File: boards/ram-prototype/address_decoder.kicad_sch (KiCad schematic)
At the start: 33 parts, among them U1 74LVC1G04, U10 74LVC1G11, U11 74LVC1G11, U2 74LVC1G04, U3 74LVC1G04, U4 74LVC1G11, U5 74LVC1G11, U6 74LVC1G11, U7 74LVC1G11, U8 74LVC1G11, U9 74LVC1G11

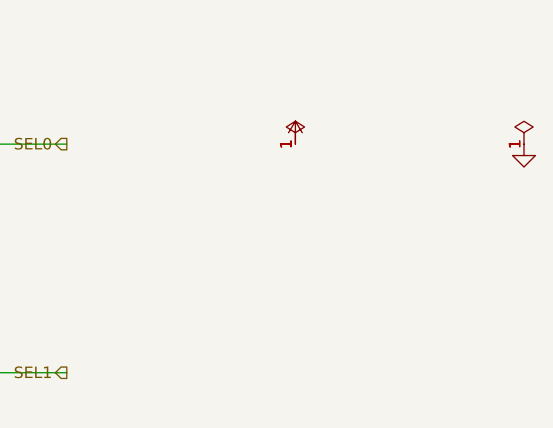
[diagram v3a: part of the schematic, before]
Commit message: More reasonable top level designrout
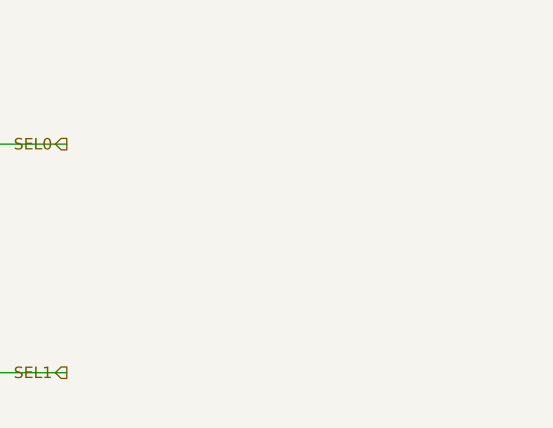
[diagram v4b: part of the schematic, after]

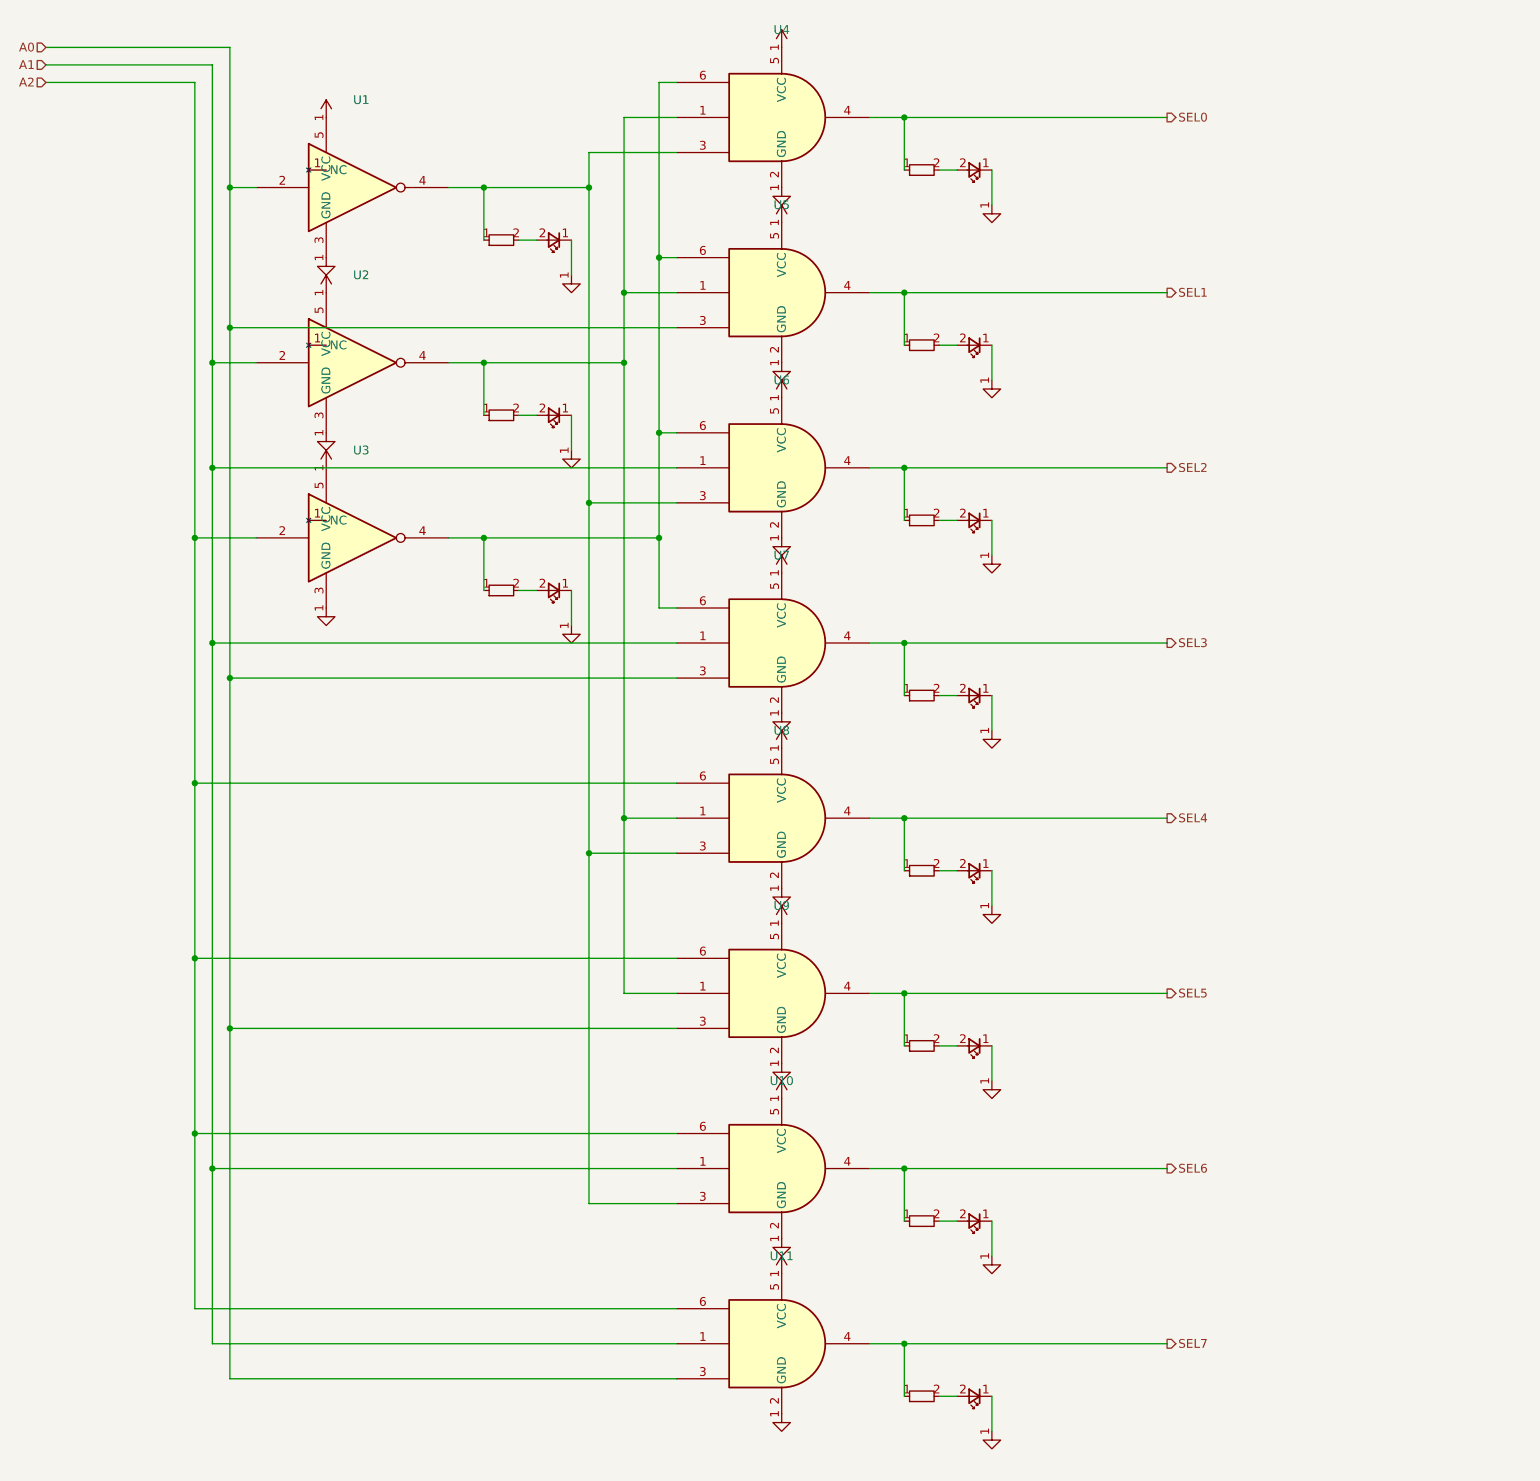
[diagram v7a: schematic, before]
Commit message: Fix labelling
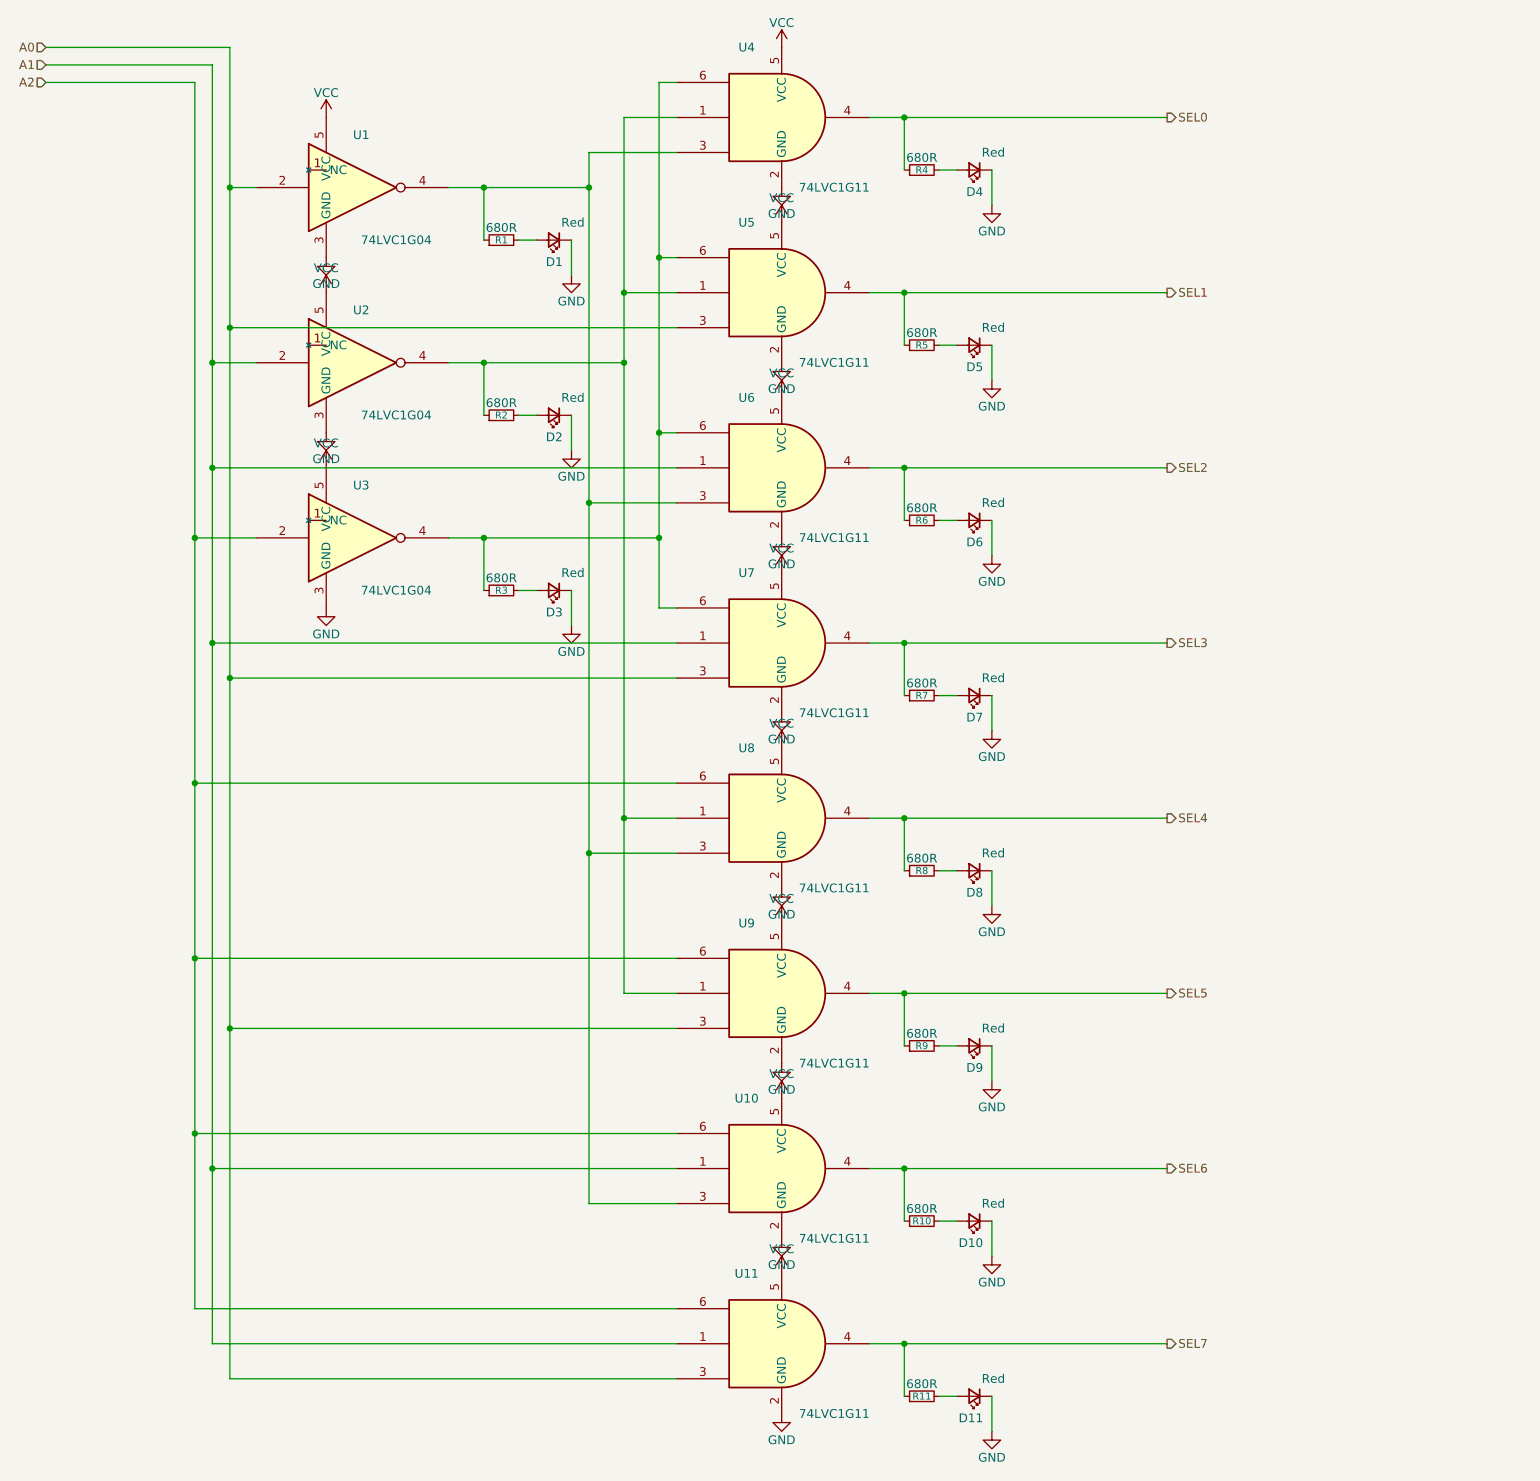
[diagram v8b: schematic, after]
